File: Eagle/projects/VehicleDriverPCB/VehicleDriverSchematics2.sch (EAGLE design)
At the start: 8 parts, among them X1 1751248

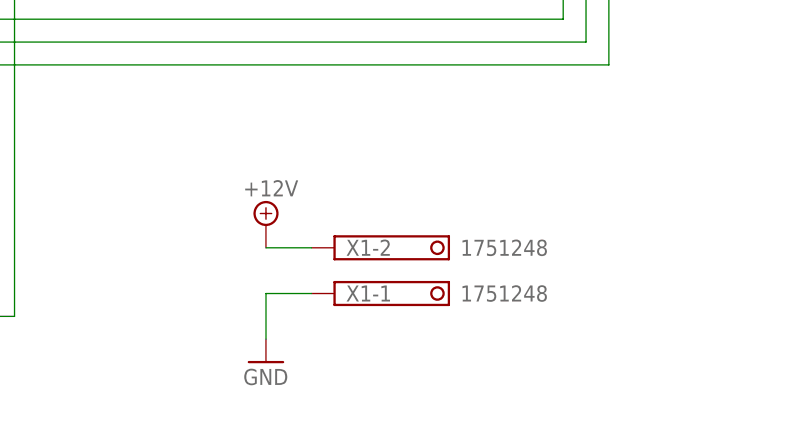
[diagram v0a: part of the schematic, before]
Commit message: Added new test project for improving in cmake, optimized PCB with new 12V terminal and silkscreen pin names
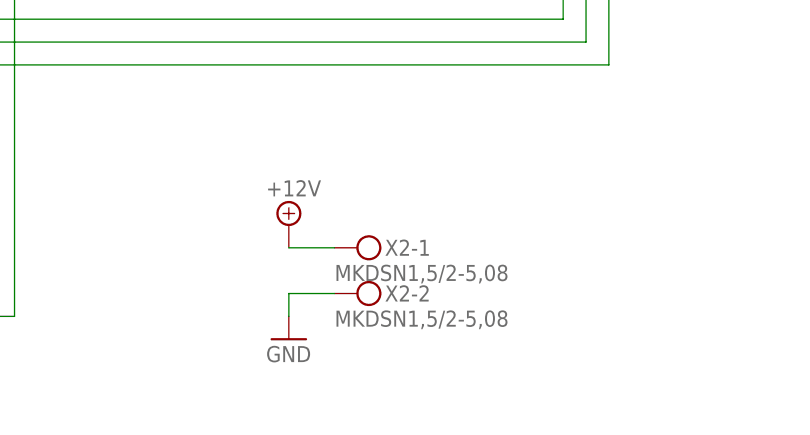
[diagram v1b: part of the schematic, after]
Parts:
- removed X1: 1751248, con-phoenix-350:1751248
- added X2: MKDSN1,5/2-5,08, con-phoenix-508:MKDSN1,5/2-5,08
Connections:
- net +12V: now also X2-1.KL; no longer X1-2.K
- net GND: now also X2-2.KL; no longer X1-1.K
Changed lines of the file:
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@@
 <part name="GND8" library="supply1" library_urn="urn:adsk.eagle:library:371" deviceset="GND" device=""/>
 <part name="P+3" library="supply1" library_urn="urn:adsk.eagle:library:371" deviceset="+5V" device=""/>
-<part name="X1" library="con-phoenix-350" library_urn="urn:adsk.eagle:library:174" deviceset="1751248" device="" package3d_urn="urn:adsk.eagle:package:9395/1"/>
-<part name="SUPPLY3" library="supply2" library_urn="urn:adsk.eagle:library:372" deviceset="+12V" device=""/>
-<part name="GND9" library="supply1" library_urn="urn:adsk.eagle:library:371" deviceset="GND" device=""/>
+<part name="X2" library="con-phoenix-508" library_urn="urn:adsk.eagle:library:176" deviceset="MKDSN1,5/2-5,08" device="" package3d_urn="urn:adsk.eagle:package:9630/1"/>
+<part name="GND10" library="supply1" library_urn="urn:adsk.eagle:library:371" deviceset="GND" device=""/>
+<part name="SUPPLY4" library="supply2" library_urn="urn:adsk.eagle:library:372" deviceset="+12V" device=""/>
 </parts>
 <sheets>
@@
 <attribute name="VALUE" x="213.36" y="53.34" size="1.778" layer="96" rot="R90"/>
 </instance>
-<instance part="X1" gate="-1" x="96.52" y="22.86" smashed="yes">
-<attribute name="NAME" x="97.79" y="21.971" size="1.778" layer="95"/>
-<attribute name="VALUE" x="110.49" y="21.971" size="1.778" layer="96"/>
-</instance>
-<instance part="X1" gate="-2" x="96.52" y="27.94" smashed="yes">
-<attribute name="NAME" x="97.79" y="27.051" size="1.778" layer="95"/>
-<attribute name="VALUE" x="110.49" y="27.051" size="1.778" layer="96"/>
-</instance>
-<instance part="SUPPLY3" gate="+12V" x="88.9" y="30.48" smashed="yes">
-<attribute name="VALUE" x="86.36" y="33.655" size="1.778" layer="96"/>
-</instance>
-<instance part="GND9" gate="1" x="88.9" y="15.24" smashed="yes">
-<attribute name="VALUE" x="86.36" y="12.7" size="1.778" layer="96"/>
+<instance part="X2" gate="-1" x="99.06" y="27.94" smashed="yes">
+<attribute name="NAME" x="102.108" y="27.051" size="1.778" layer="95"/>
+<attribute name="VALUE" x="96.52" y="24.257" size="1.778" layer="96"/>
+</instance>
+<instance part="X2" gate="-2" x="99.06" y="22.86" smashed="yes">
+<attribute name="NAME" x="102.108" y="21.971" size="1.778" layer="95"/>
+<attribute name="VALUE" x="96.52" y="19.177" size="1.778" layer="96"/>
+</instance>
+<instance part="GND10" gate="1" x="91.44" y="17.78" smashed="yes">
+<attribute name="VALUE" x="88.9" y="15.24" size="1.778" layer="96"/>
+</instance>
+<instance part="SUPPLY4" gate="+12V" x="91.44" y="30.48" smashed="yes">
+<attribute name="VALUE" x="88.9" y="33.655" size="1.778" layer="96"/>
 </instance>
 </instances>
@@
 </segment>
 <segment>
-<pinref part="GND9" gate="1" pin="GND"/>
-<wire x1="88.9" y1="17.78" x2="88.9" y2="22.86" width="0.1524" layer="91"/>
-<pinref part="X1" gate="-1" pin="K"/>
-<wire x1="88.9" y1="22.86" x2="93.98" y2="22.86" width="0.1524" layer="91"/>
+<pinref part="GND10" gate="1" pin="GND"/>
+<wire x1="91.44" y1="20.32" x2="91.44" y2="22.86" width="0.1524" layer="91"/>
+<pinref part="X2" gate="-2" pin="KL"/>
+<wire x1="91.44" y1="22.86" x2="96.52" y2="22.86" width="0.1524" layer="91"/>
 </segment>
 </net>
@@
 </segment>
 <segment>
-<pinref part="SUPPLY3" gate="+12V" pin="+12V"/>
-<pinref part="X1" gate="-2" pin="K"/>
-<wire x1="88.9" y1="27.94" x2="93.98" y2="27.94" width="0.1524" layer="91"/>
-</segment>
-<segment>
 <pinref part="U$8" gate="G$1" pin="VIN"/>
 <wire x1="30.48" y1="20.32" x2="30.48" y2="15.24" width="0.1524" layer="91"/>
@@
 <wire x1="12.7" y1="15.24" x2="30.48" y2="15.24" width="0.1524" layer="91"/>
 </segment>
+<segment>
+<pinref part="SUPPLY4" gate="+12V" pin="+12V"/>
+<pinref part="X2" gate="-1" pin="KL"/>
+<wire x1="91.44" y1="27.94" x2="96.52" y2="27.94" width="0.1524" layer="91"/>
+</segment>
 </net>
